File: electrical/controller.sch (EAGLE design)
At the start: 31 parts, among them Q1 IRLIB9343PBF-ND, U1 POLOLU_D24V22F5, U2 TPS3710, U3 MCP4725, U4 MCP4725, U5 MCP6002

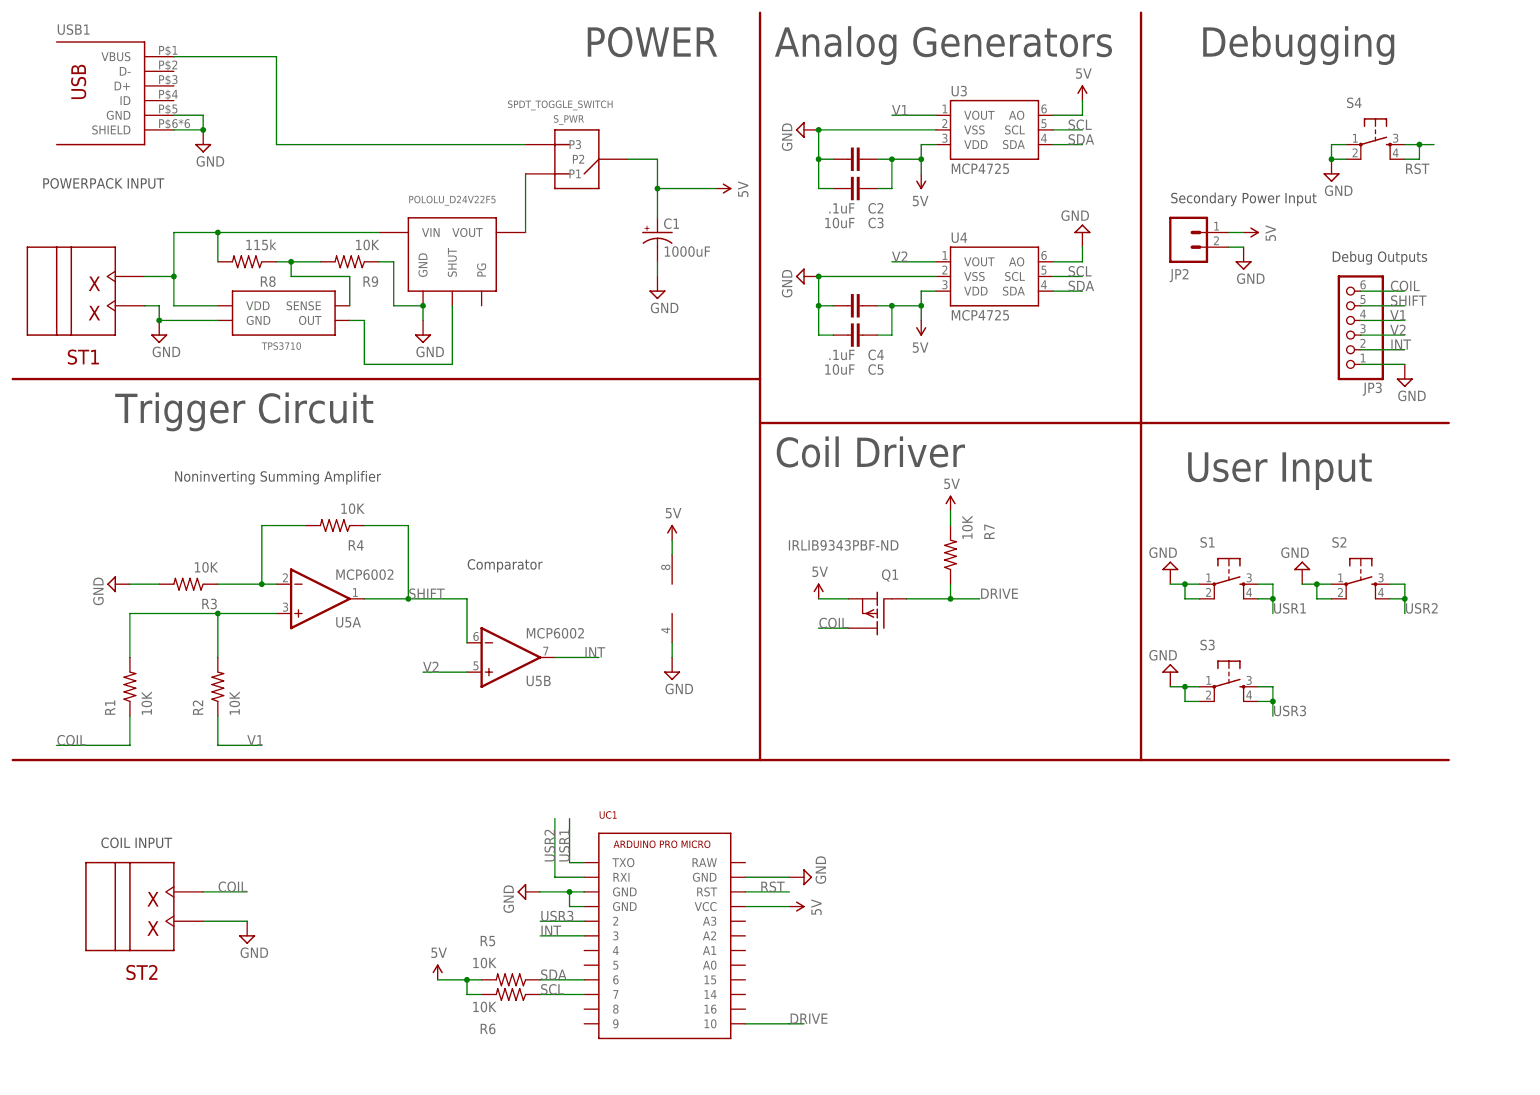
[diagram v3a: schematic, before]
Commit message: Finally reasonable progress on the electronics
This plus github.

Nearly done fleshing the SCH out.

Routing should not be difficult, just a few hours.

Postponing changing the power parts of this circuit untill after the
spools are done.  Everything but the power, I can do now --> ship a
revision, test it.
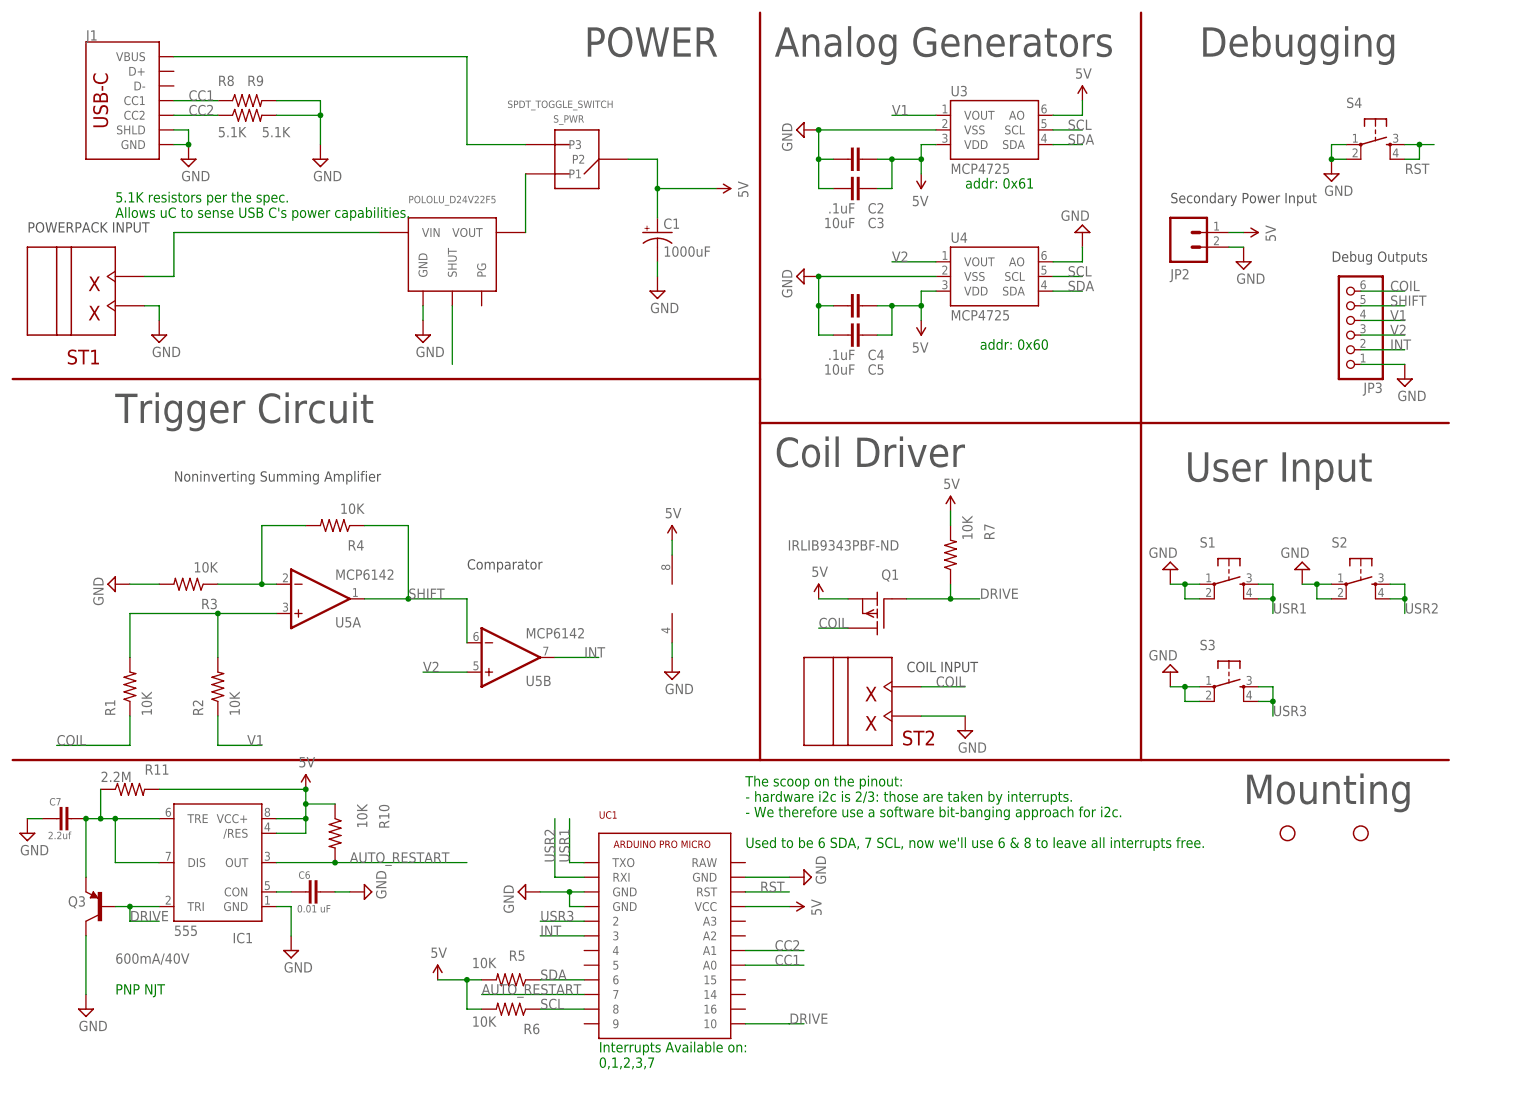
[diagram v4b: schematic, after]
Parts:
- removed U2: TPS3710, custom_parts:TPS3710
- removed USB1: USB-OTGMICRO-AB, pie:USB-OTGMICRO-AB
- added C6: 0.01 uF, BEST_Custom:CAP0603-CAP
- added C7: 2.2uf, BEST_Custom:CAP0603-CAP
- added IC1: 555, SparkFun-IC-Special-Function:555D
- added J1: (no value), SparkFun-Connectors:USB_C_2-LAYER_PADS
- added Q3: 600mA/40V, SparkFun-DiscreteSemi:TRANS_PNP-MMBT4403
- added R10: 10K, pie:R-US_R0603
- added R11: 2.2M, pie:R-US_R0603
- added STANDOFF1, STANDOFF2: STAND-OFFKEYSTONE_SMT_STANDOFF, BEST_Custom:STAND-OFFKEYSTONE_SMT_STANDOFF
- R8: value 115k -> 5.1K
- R9: value 10K -> 5.1K
- U5: value MCP6002 -> MCP6142
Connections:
- new net AUTO_RESTART: IC1.OUT, R10.2, UC1.7
- new net CC1: J1.CC1, R8.1, UC1.A0
- new net CC2: J1.CC2, R9.1, UC1.A1
- new net N$7: C7.2, IC1.DIS, IC1.TRE, Q3.E, R11.1
- net 5V: now also IC1./RES, IC1.VCC+, R10.1, R11.2
- net DRIVE: now also IC1.TRI, Q3.B
- net GND: now also C6.2, C7.1, IC1.GND, J1.GND, J1.SHLD, Q3.C, R8.2, R9.2; no longer R9.1, U2.GND, USB1.GND, USB1.SHIELD
- net N$1: no longer U2.OUT
- net N$2: now also J1.VBUS; no longer USB1.VBUS
- net N$6: now also C6.1, IC1.CON; no longer R8.1, R9.2, U2.SENSE
- net SCL: now also UC1.8; no longer UC1.7
- net VBAT: no longer R8.2, U2.VDD
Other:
- note added: "5.1K resistors per the spec. Allows uC to sense USB C's power capabilities."
- note added: "Interrupts Available on: 0,1,2,3,7"
- note added: "Mounting"
- note added: "PNP NJT"
- note added: "The scoop on the pinout: - hardware i2c is 2/3: those are taken by interrupts. - We therefore use a software bit-banging approach for i2c. Used to be 6 SDA, 7 SCL, now we'll use 6 & 8 to leave all interrupts free."
- note added: "addr: 0x60"
- note added: "addr: 0x61"
- moved on the sheet: R6, R8, R9, ST2

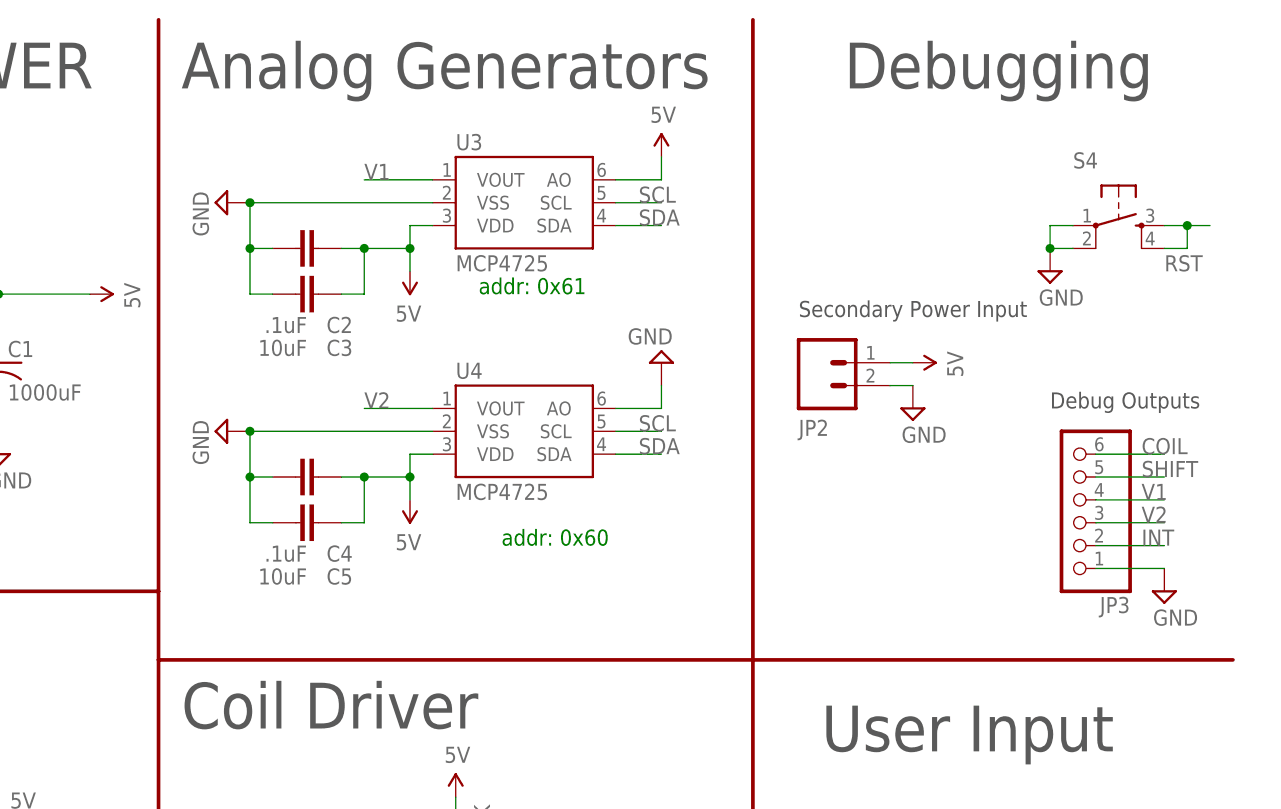
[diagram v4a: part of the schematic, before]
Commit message: Finish rev D1
Most of hte new features, except without overhauling the power system
b/c the power system requires tests with spools, which I havent done
yet.
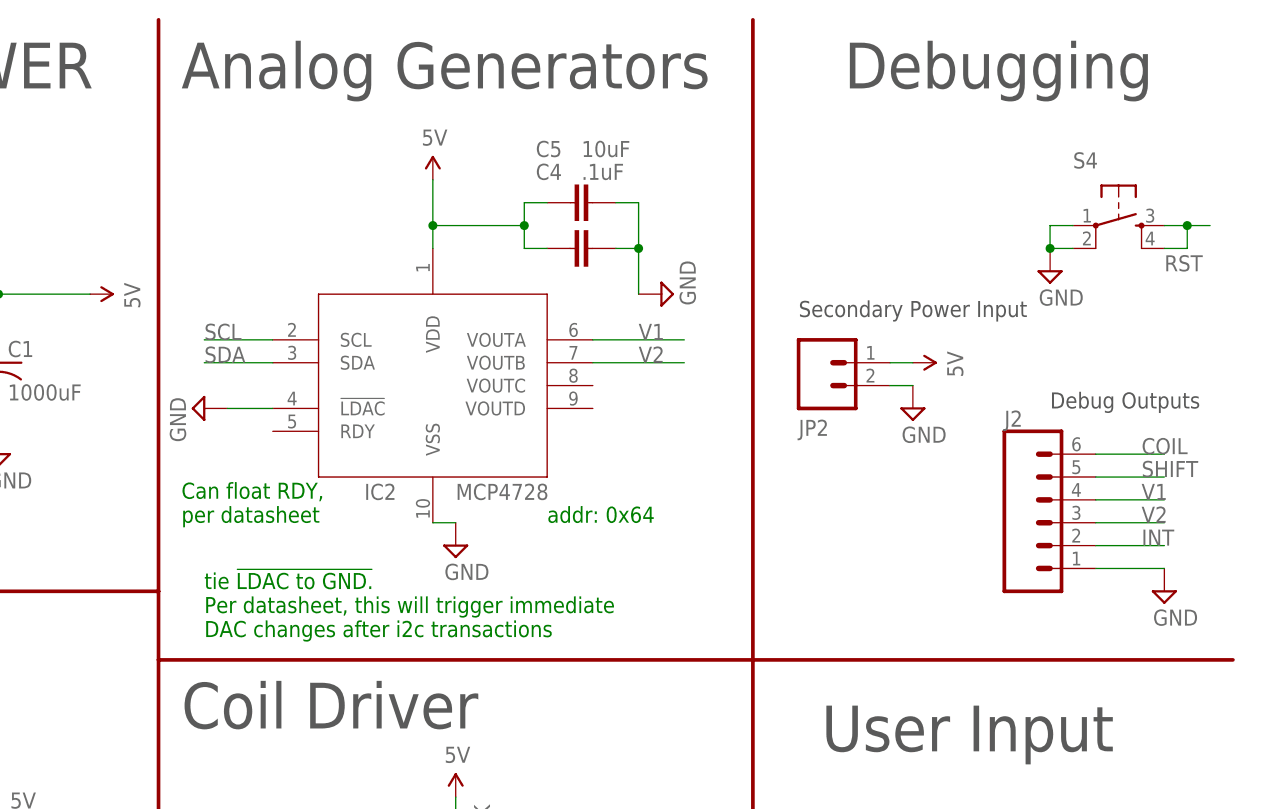
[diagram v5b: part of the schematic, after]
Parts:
- removed C2: .1uF, pie:CAP0603-CAP
- removed C3: 10uF, pie:CAP0805
- removed JP3: (no value), pinhead:PINHD-1X6
- removed U3, U4: MCP4725, SparkFun-AnalogIC:MCP4725SOT-23
- added IC2: MCP4728, BEST_Custom:MCP4728
- added J2: (no value), SparkFun-Connectors:CONN_06NO_SILK_FEMALE_PTH
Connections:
- net 5V: now also IC2.VDD; no longer C2.1, C3.1, U3.AO, U3.VDD, U4.VDD
- net COIL: now also J2.6; no longer JP3.6
- net GND: now also IC2.!LDAC, IC2.VSS, J2.1; no longer C2.2, C3.2, JP3.1, U3.VSS, U4.AO, U4.VSS
- net INT: now also J2.2; no longer JP3.2
- net SCL: now also IC2.SCL; no longer U3.SCL, U4.SCL
- net SDA: now also IC2.SDA; no longer U3.SDA, U4.SDA
- net SHIFT: now also J2.5; no longer JP3.5
- net V1: now also IC2.VOUTA, J2.4; no longer JP3.4, U3.VOUT
- net V2: now also IC2.VOUTB, J2.3; no longer JP3.3, U4.VOUT
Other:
- note added: "Can float RDY, per datasheet"
- note added: "addr: 0x64"
- note added: "tie !LDAC to GND. Per datasheet, this will trigger immediate DAC changes after i2c transactions"
- note removed: "addr: 0x60"
- note removed: "addr: 0x61"
- moved on the sheet: C4, C5
